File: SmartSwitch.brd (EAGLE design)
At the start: 100 x 50 mm, 24 parts

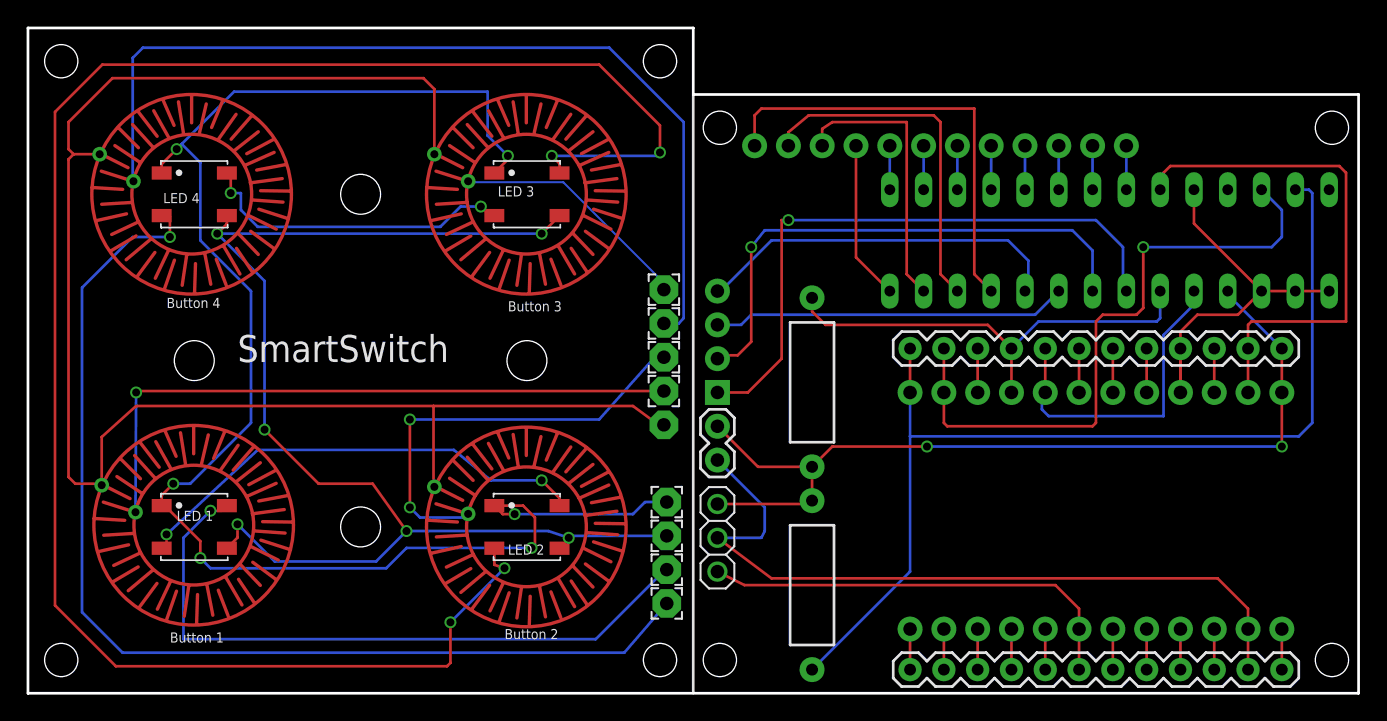
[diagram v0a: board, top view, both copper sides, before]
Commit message: Update WS2812B Positions
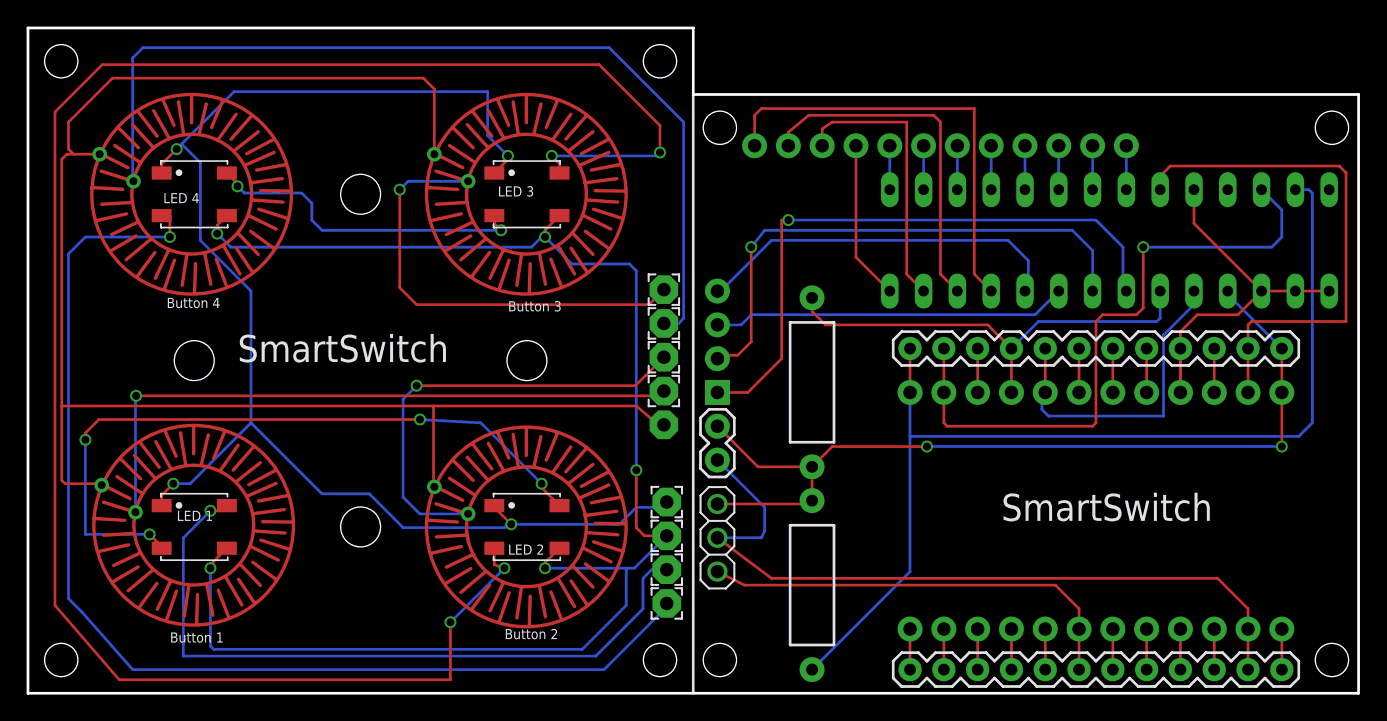
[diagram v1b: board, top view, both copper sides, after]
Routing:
- net GROUND: track 96.0 -> 114.3 mm, vias 6 -> 5
- net N$11: track 35.1 -> 52.7 mm, vias 2 -> 4
- net N$4: track 18.8 -> 33.6 mm, vias 0 -> 1
- net N$10: track 118.0 -> 104.7 mm, vias 6 -> 4
- net N$9: track 81.6 -> 85.8 mm
- net MOSI: track 50.4 -> 53.6 mm
- net N$12: track 140.3 -> 142.1 mm
- net N$2: track 32.6 -> 33.7 mm, vias 2 -> 1

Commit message: Change GND/VCC on Buttonpad connection
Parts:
- moved JP2 2.54 mm to (51.8, 20.1), turned to 270 degrees
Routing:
- net N$30: track 57.1 -> 62.5 mm
- net N$28: track 67.4 -> 62.4 mm
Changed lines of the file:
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@@
 <hole x="98" y="42.5" drill="2.5"/>
 <hole x="98" y="2.5" drill="2.5"/>
-<text x="57.15" y="19.558" size="1.27" layer="26" rot="MR0">VCC</text>
-<text x="57.404" y="16.764" size="1.27" layer="26" rot="MR0">GND</text>
+<text x="57.15" y="16.51" size="1.27" layer="26" rot="MR0">VCC</text>
+<text x="57.15" y="19.05" size="1.27" layer="26" rot="MR0">GND</text>
 <hole x="52" y="42.5" drill="2.5"/>
 <hole x="52" y="2.5" drill="2.5"/>
@@
 <attribute name="VALUE" x="47.792" y="19.174" size="0.0254" layer="28" rot="MR180"/>
 </element>
-<element name="JP2" library="SparkFun-Connectors" package="1X02" value="M02PTH" x="51.816" y="17.526" smashed="yes" rot="R90"/>
+<element name="JP2" library="SparkFun-Connectors" package="1X02" value="M02PTH" x="51.816" y="20.066" smashed="yes" rot="R270"/>
 </elements>
 <signals>
@@
 <wire x1="58.928" y1="14.478" x2="58.674" y2="14.224" width="0.2032" layer="1"/>
 <wire x1="58.674" y1="14.224" x2="51.816" y2="14.224" width="0.2032" layer="1"/>
-<wire x1="51.816" y1="20.066" x2="54.864" y2="17.018" width="0.2032" layer="1"/>
-<wire x1="54.864" y1="17.018" x2="58.928" y2="17.018" width="0.2032" layer="1"/>
+<wire x1="51.816" y1="17.526" x2="51.816" y2="14.224" width="0.2032" layer="1"/>
 </signal>
 <signal name="N$29">
@@
 <wire x1="55.88" y1="8.636" x2="51.816" y2="11.684" width="0.2032" layer="1"/>
 <contactref element="JP2" pad="1"/>
-<wire x1="51.816" y1="17.526" x2="55.372" y2="13.97" width="0.2032" layer="16"/>
-<wire x1="55.372" y1="13.97" x2="55.372" y2="12.192" width="0.2032" layer="16"/>
-<wire x1="55.372" y1="12.192" x2="55.118" y2="11.684" width="0.2032" layer="16"/>
-<wire x1="55.118" y1="11.684" x2="51.816" y2="11.684" width="0.2032" layer="16"/>
+<wire x1="51.816" y1="11.684" x2="55.372" y2="11.684" width="0.2032" layer="16"/>
+<wire x1="55.372" y1="11.684" x2="55.88" y2="12.192" width="0.2032" layer="16"/>
+<wire x1="55.88" y1="12.192" x2="55.88" y2="19.812" width="0.2032" layer="16"/>
+<wire x1="55.88" y1="19.812" x2="55.626" y2="20.066" width="0.2032" layer="16"/>
+<wire x1="55.626" y1="20.066" x2="51.816" y2="20.066" width="0.2032" layer="16"/>
 </signal>
 <signal name="N$32">

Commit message: Move resistors
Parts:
- moved R2 22.3 mm to (80.3, 17.0), flipped to the bottom, turned to 0 degrees
- moved R1 21.5 mm to (80.3, 10.9), flipped to the bottom, turned to 0 degrees
- renumbered BUTTON1 to BTN1, BUTTON2 to BTN2, BUTTON3 to BTN3, BUTTON4 to BTN4
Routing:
- net N$28: track 62.4 -> 82.8 mm, vias 2 -> 0
- net N$51: track 34.6 -> 23.0 mm
- net N$34: track 76.5 -> 71.9 mm
- net N$33: vias 1 -> 2
